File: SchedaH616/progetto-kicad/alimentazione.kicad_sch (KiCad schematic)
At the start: 62 parts, among them J103 DC-005-5A-2.0, J104 TYPE-C-31-M-12, U101 TPS56637RPAR, U103 TPS2121RUXR, U104 FUSB302BMPX, U105 SY6280AAC, U107 TPD2EUSB30ADRTR, U108 TPS2121RUXR

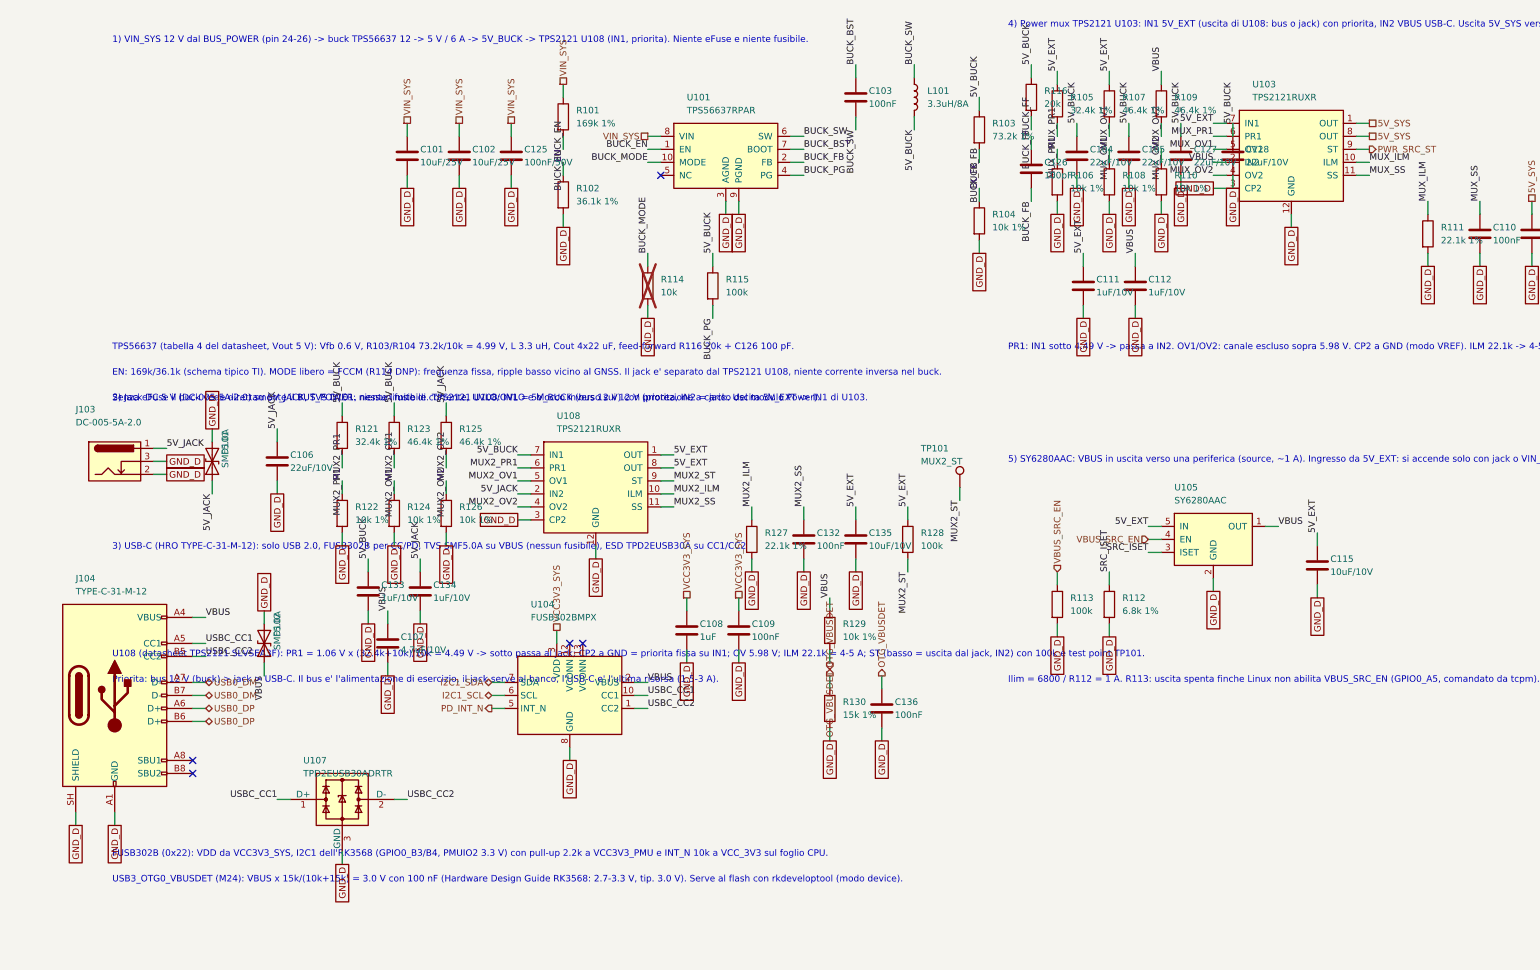
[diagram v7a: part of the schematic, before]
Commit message: SchedaH616: componenti specifici dalla libreria MIKILAB
- simbolo e footprint MIKILAB per RK809-5, TCS4525, K4AAG165WA-BCWE, FEMDNN064G-C9A61,
  AP2112K-1.8TRG1, TPS56637RPAR, TPS2121RUXR, SY6280AAC, TPS563201DDCR, TPS2553DBVR,
  TYPE-C-31-M-12, FH12-30S-0.5SH, FPC-05F-28PH20, HR911130C, 25AA02E48T-I/OT, DM3AT-SF-PEJM5;
  simbolo MIKILAB per l'AP6256
- restano nella libreria di progetto: RK3568 (pad EasyEDA da 0.35 mm, niente fanout 5/5 mil),
  simbolo RTL8211F (quello MIKILAB ha pin di alimentazione nascosti), footprint AP6256 LGA-47,
  portapila BS-12; motivazioni in docs/scelte-progetto.md
- kilib.mik() carica simboli e footprint dalla libreria (variabile MIKILAB); matrice ERC:
  pin unspecified dei simboli EasyEDA OK
- netlist identica a 4ca35fc (439 componenti, 314 net); ERC 0, parita' 0, DRC 0 (solo
  collegamenti da fare); footprint corretti nella libreria MIKILAB 8b990c4

Co-Authored-By: Claude Opus 5.5 (1M context) <noreply@anthropic.com>
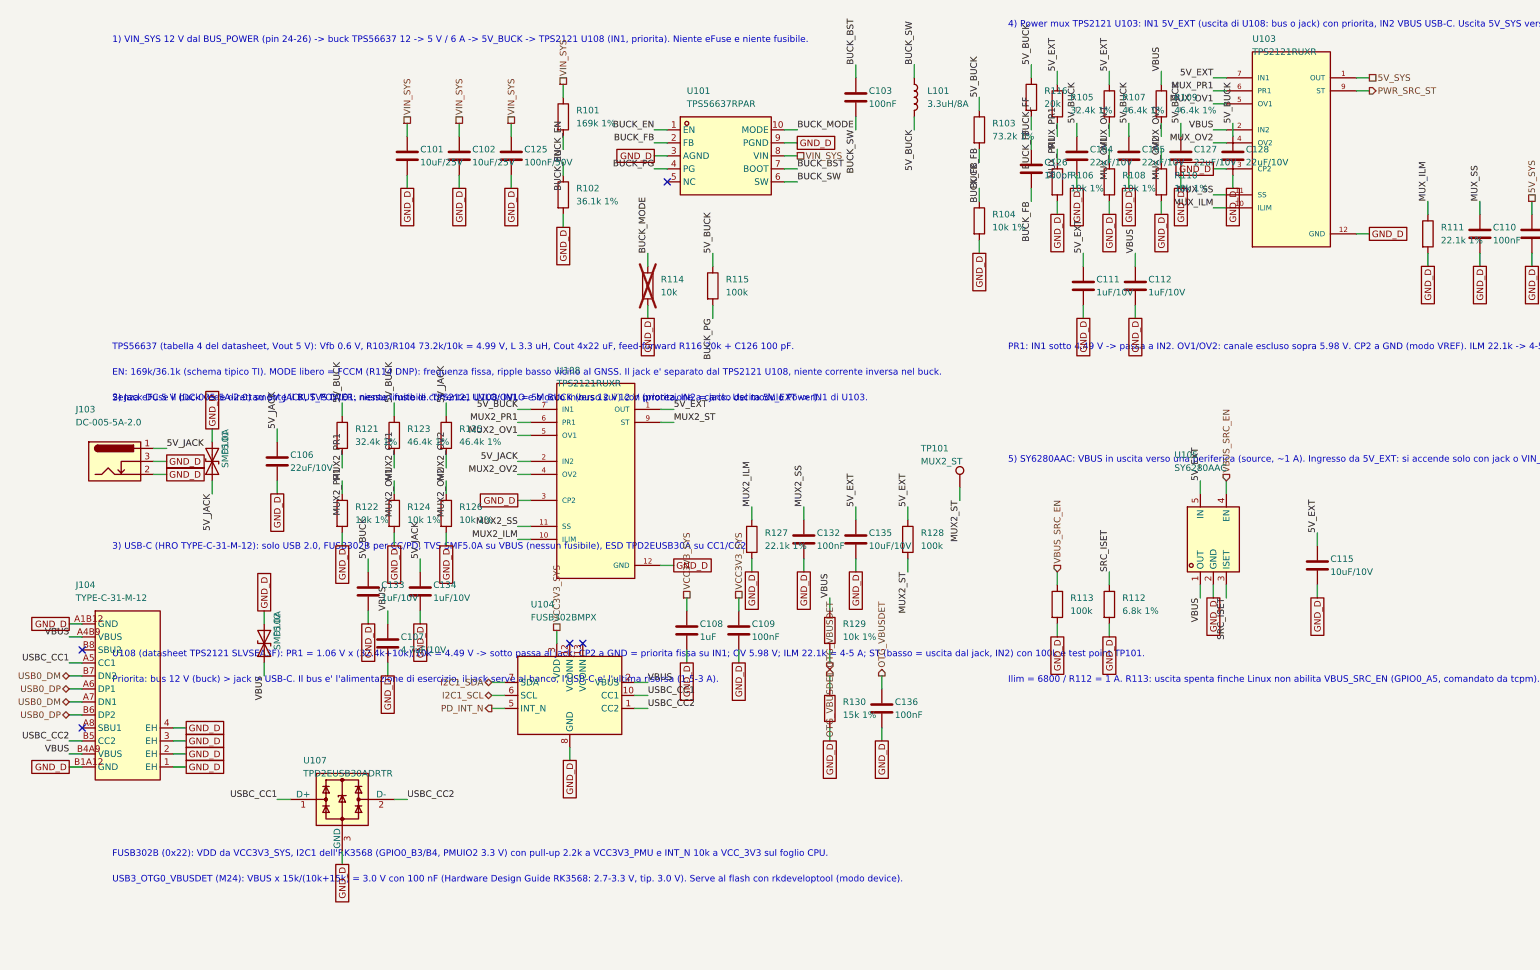
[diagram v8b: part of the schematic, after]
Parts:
- removed J104: TYPE-C-31-M-12, Connector_USB:USB_C_Receptacle_HRO_TYPE-C-31-M-12, symbol Connector:USB_C_Receptacle_USB2.0_16P
- removed U101: TPS56637RPAR, Scheda:Texas_RPA0010A_VQFN-HR-10_3x3mm, symbol Scheda:TPS56637
- removed U103, U108: TPS2121RUXR, Package_DFN_QFN:Texas_VQFN-HR-12_2x2.5mm_P0.5mm, symbol Scheda:TPS2121
- removed U105: SY6280AAC, Package_TO_SOT_SMD:SOT-23-5, symbol Scheda:SY6280AAC
- added J104: TYPE-C-31-M-12, MIKILAB_TYPE_C_31_M_12:USB-C_SMD-TYPE-C-31-M-12_1, symbol MIKILAB_TYPE_C_31_M_12:TYPE-C-31-M-12
- added U101: TPS56637RPAR, MIKILAB_TPS56637RPAR:VQFN-HR-10_L3.0-W3.0_RPA, symbol MIKILAB_TPS56637RPAR:TPS56637RPAR
- added U103, U108: TPS2121RUXR, MIKILAB_TPS2121RUXR:IC_TPS2121RUXR, symbol MIKILAB_TPS2121RUXR:TPS2121RUXR
- added U105: SY6280AAC, MIKILAB_SY6280AAC:SOT-23-5_L3.0-W1.7-P0.95-LS2.8-BL, symbol MIKILAB_SY6280AAC:SY6280AAC
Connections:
- net 5V_BUCK: now also U108.7 (IN1), U108.7_1 (IN1)
- net 5V_EXT: now also U103.7 (IN1), U103.7_1 (IN1), U105.5 (IN), U108.1 (OUT), U108.1_1 (OUT), U108.8 (OUT), U108.8_1 (OUT)
- net 5V_JACK: now also U108.2 (IN2), U108.2_1 (IN2)
- net 5V_SYS: now also U103.1 (OUT), U103.1_1 (OUT), U103.8 (OUT), U103.8_1 (OUT)
- net BUCK_BST: now also U101.7 (BOOT)
- net BUCK_EN: now also U101.1 (EN)
- net BUCK_FB: now also U101.2 (FB)
- net BUCK_MODE: now also U101.10 (MODE)
- net BUCK_PG: now also U101.4 (PG)
- net BUCK_SW: now also U101.6 (SW)
- net GND_D: now also J104.1 (EH), J104.2 (EH), J104.3 (EH), J104.4 (EH), J104.A1B12 (GND), J104.B1A12 (GND), U101.3 (AGND), U101.9 (PGND), U103.12 (GND), U103.3 (CP2), U105.2 (GND), U108.12 (GND), U108.3 (CP2)
- net MUX2_ILM: now also U108.10 (ILIM)
- net MUX2_OV1: now also U108.5 (OV1)
- net MUX2_OV2: now also U108.4 (OV2)
- net MUX2_PR1: now also U108.6 (PR1)
- net MUX2_SS: now also U108.11 (SS)
- net MUX2_ST: now also U108.9 (ST)
- net MUX_ILM: now also U103.10 (ILIM)
- net MUX_OV1: now also U103.5 (OV1)
- net MUX_OV2: now also U103.4 (OV2)
- net MUX_PR1: now also U103.6 (PR1)
- net MUX_SS: now also U103.11 (SS)
- net PWR_SRC_ST: now also U103.9 (ST)
- net SRC_ISET: now also U105.3 (ISET)
- net USB0_DM: now also J104.A7 (DN1), J104.B7 (DN2)
- net USB0_DP: now also J104.A6 (DP1), J104.B6 (DP2)
- net USBC_CC1: now also J104.A5 (CC1)
- net USBC_CC2: now also J104.B5 (CC2)
- net VBUS: now also J104.A4B9 (VBUS), J104.B4A9 (VBUS), U103.2 (IN2), U103.2_1 (IN2), U105.1 (OUT)
- net VBUS_SRC_EN: now also U105.4 (EN)
- net VIN_SYS: now also U101.8 (VIN)
